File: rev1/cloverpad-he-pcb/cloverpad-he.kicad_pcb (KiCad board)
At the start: 2 copper layers, 70 x 75 mm, 51 parts, among them J1 USB_C_Receptacle_USB2.0, SW1 SW_Push, SW2 SW_Push, U1 SRV05-4, U2 XC6206P332MR, U3 DRV5056A4xDBZxQ1, U4 DRV5056A4xDBZxQ1, U5 DRV5056A4xDBZxQ1, U8 RP2040, U9 W25Q16JVSSIQ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

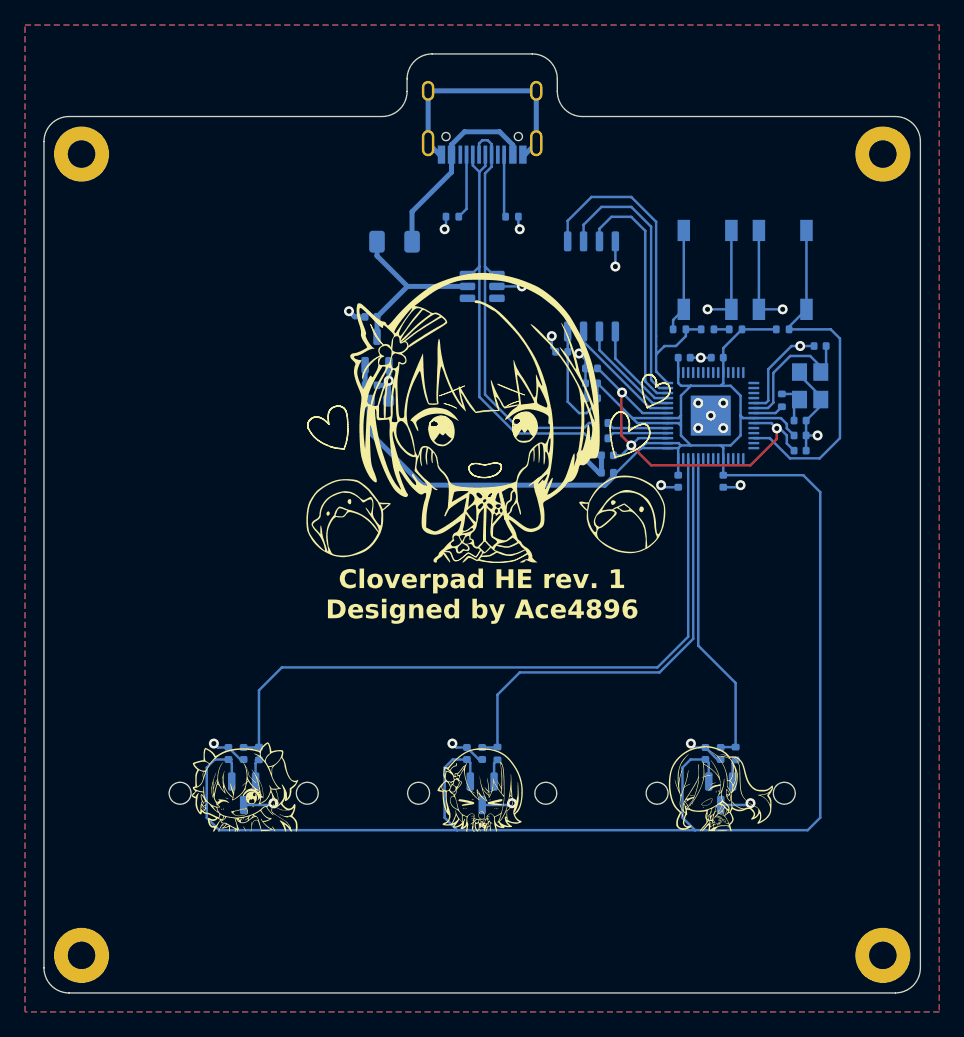
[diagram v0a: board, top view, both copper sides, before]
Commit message: fix: use DRV5056A3 instead of A4
after some testing, losing the bottom 0.2mm of travel isn't a huge problem, and it's better to increase the resolution for the upper part of the keystroke instead.
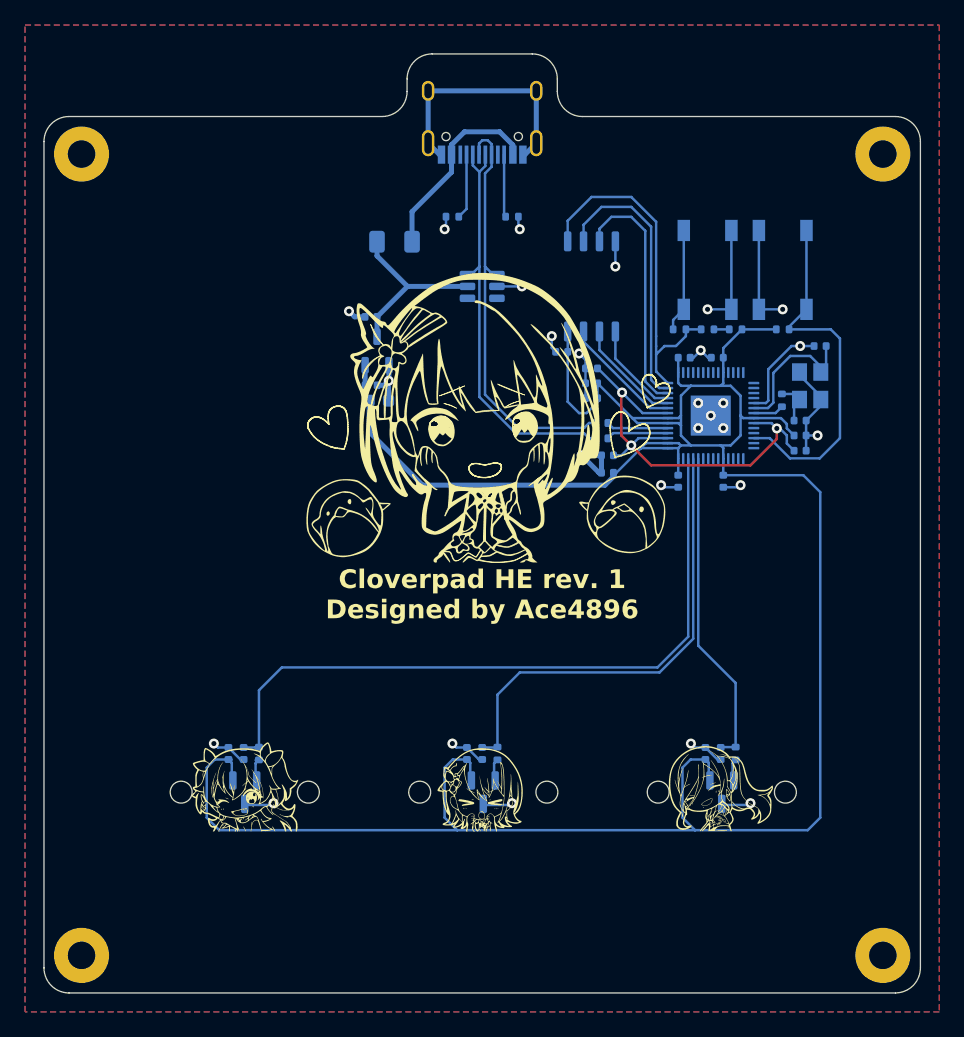
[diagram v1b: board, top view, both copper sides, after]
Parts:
- U3, U4, U5: value DRV5056A4xDBZxQ1 -> DRV5056AxxDBZxQ1
- moved U3 0.12 mm to (41.8, 79.8)
- moved U4 0.12 mm to (60.9, 79.8)
- moved U5 0.12 mm to (79.9, 79.8)

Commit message: chore: update all symbols + footprints to match kicad 8
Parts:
- C1, C12, C16, C2, C28, C3, C4, C5, C6, C7, C8: value 1uF -> C_Small
- C13, C14, C17, C18, C19, C20, C21, C22, C23: value 100nF -> C_Small
- C15: value 10uF -> C_Small
- C24, C25: value 22pF -> C_Small
- F1: value 500mA -> Polyfuse_Small
- H1, H2, H3, H4: value Mounting Hole -> MountingHole_Pad
- J1: value USB_C_Receptacle_USB2.0 -> USB_C_Receptacle_USB2.0_16P
- R1, R10, R12, R13, R2: value 5k1 -> R_Small
- R11, R9: value 27 -> R_Small
- R14, R7: value 1k -> R_Small
- R3, R4, R5: value 100 -> R_Small
- U2: value XC6206P332MR -> XC6206PxxxMR
- U9: value W25Q16JVSSIQ -> W25Q128JVS
- Y1: value 12MHz -> Crystal_GND24
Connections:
- U8 pad 24: SWCLK -> unconnected-(U8-SWCLK-Pad24)
- U8 pad 25: SWD -> unconnected-(U8-SWD-Pad25)
